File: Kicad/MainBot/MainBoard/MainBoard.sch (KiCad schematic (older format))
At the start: 58 parts, among them J1 Conn_01x02, J10 Conn_01x24, J11 01x24, J12 Conn_01x05, J13 Conn_01x03, J14 Conn_01x03, J15 Conn_01x03, J16 01x04, J17 01x04, J18 01x04, J19 01x04, J20 Conn_01x03, U1 AZ1117-3.3, U2 TCA9548A, U3 Teensy3.6, U4 DRV8825, U5 DRV8825, U6 DRV8825, U7 DRV8825

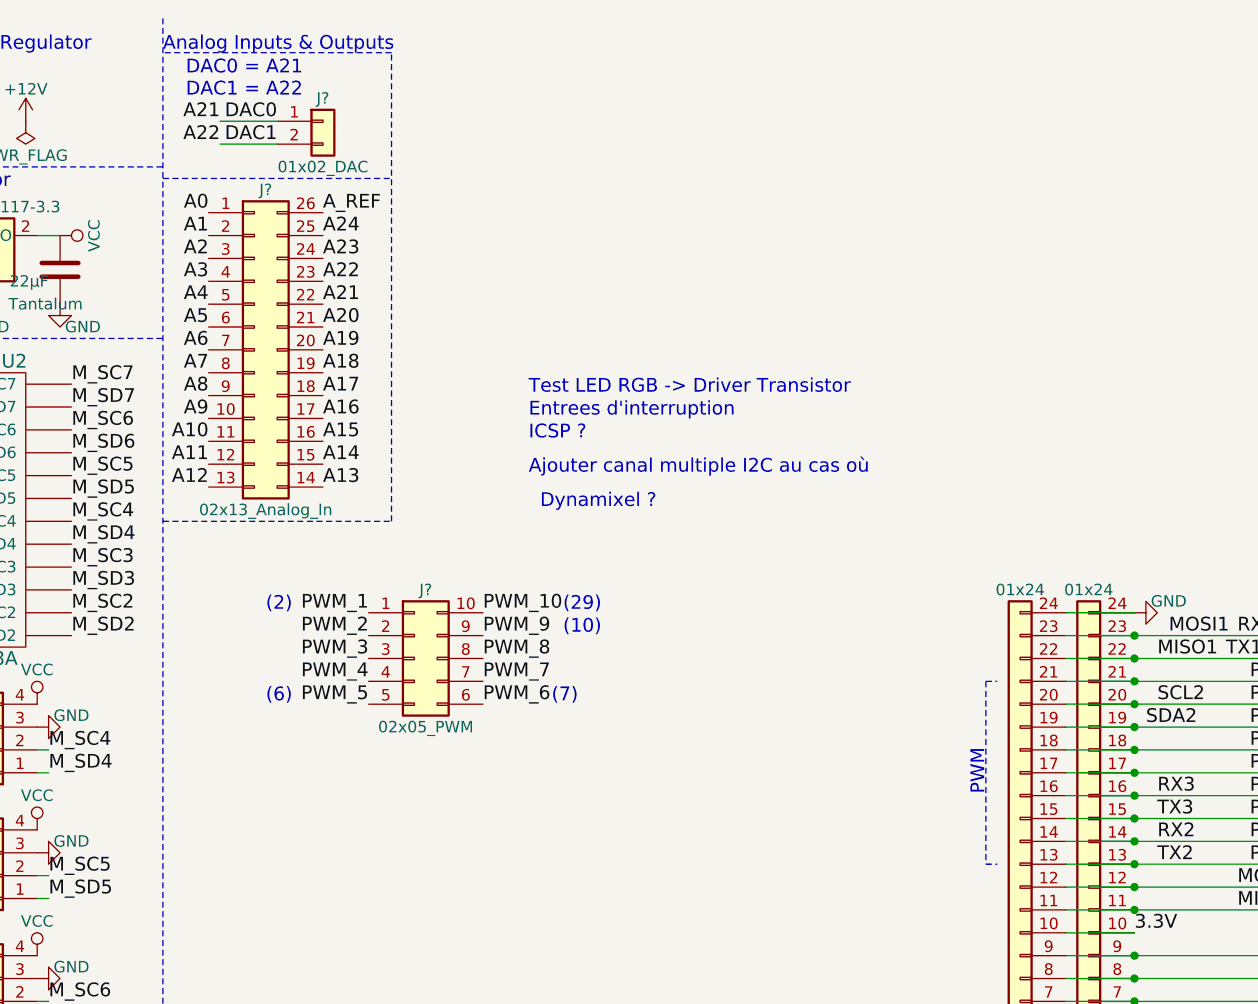
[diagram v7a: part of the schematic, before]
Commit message: Deleted PWM and analog blocks
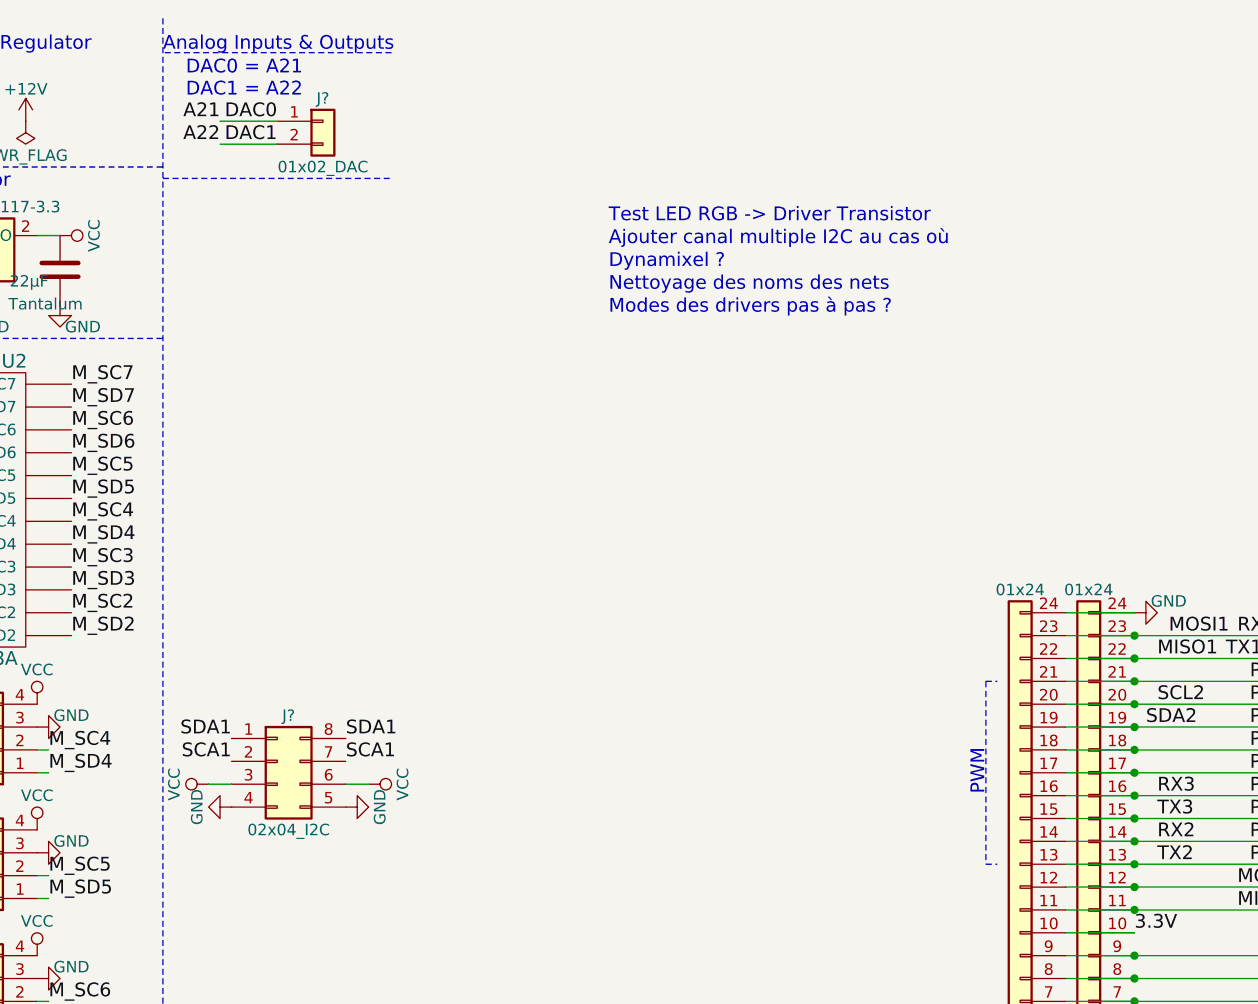
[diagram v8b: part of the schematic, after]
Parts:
- removed J?: 02x13_Analog_In, symbol Conn_02x13_Counter_Clockwise
- removed J?: 02x05_PWM, symbol Conn_02x05_Counter_Clockwise
- added J?: 02x04_I2C, symbol Conn_02x04_Counter_Clockwise
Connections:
- net A19: now also J?.1 (Pin_1), J?.8 (Pin_8)
- net GND: now also J?.4 (Pin_4), J?.5 (Pin_5)
- net VCC: now also J?.3 (Pin_3), J?.6 (Pin_6)
- new net SCA1: J?.2 (Pin_2), J?.7 (Pin_7)
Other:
- note added: "Modes des drivers pas à pas ?\n"
- note added: "Nettoyage des noms des nets\n"
- note removed: "(10)\n"
- note removed: "(2)\n"
- note removed: "(29)\n"
- note removed: "(6)\n"
- note removed: "(7)\n"
- note removed: "Entrees d'interruption\n"
- note removed: "ICSP ?\n"
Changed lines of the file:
@@
 Text Label 850  9400 0    60   ~ 0
 3.3V
-Text Notes 3850 2250 0    60   ~ 0
-Entrees d'interruption\n
-Text Notes 3850 2350 0    60   ~ 0
-ICSP ?\n
-Text Notes 3850 2150 0    60   ~ 0
+Text Notes 4200 1400 0    60   ~ 0
 Test LED RGB -> Driver Transistor\n
 $Comp
@@
 Wire Wire Line
 	9300 6100 9900 6100
-Text Label 2450 1350 2    60   ~ 0
-A0
-Text Label 2450 1450 2    60   ~ 0
-A1
-Text Label 2450 1550 2    60   ~ 0
-A2
-Text Label 2450 1650 2    60   ~ 0
-A3
-Text Label 2450 1750 2    60   ~ 0
-A4
-Text Label 2450 1850 2    60   ~ 0
-A5
-Text Label 2450 1950 2    60   ~ 0
-A6
-Text Label 2450 2050 2    60   ~ 0
-A7
-Text Label 2450 2150 2    60   ~ 0
-A8
-Text Label 2450 2250 2    60   ~ 0
-A9
-Text Label 2450 2350 2    60   ~ 0
-A10
-Text Label 2450 2450 2    60   ~ 0
-A11
-Text Label 2450 2550 2    60   ~ 0
-A12
-Text Label 2950 2550 0    60   ~ 0
-A13
-Text Label 2950 2450 0    60   ~ 0
-A14
-Text Label 2950 2350 0    60   ~ 0
-A15
-Text Label 2950 2250 0    60   ~ 0
-A16
-Text Label 2950 2150 0    60   ~ 0
-A17
-Text Label 2950 2050 0    60   ~ 0
-A18
-Text Label 2950 1950 0    60   ~ 0
-A19
-Text Label 2950 1850 0    60   ~ 0
-A20
-Text Label 2950 1750 0    60   ~ 0
-A21
-Text Label 2950 1650 0    60   ~ 0
-A22
-Text Label 2950 1550 0    60   ~ 0
-A23
-$Comp
-L Conn_02x13_Counter_Clockwise J?
-U 1 1 5C64862D
-P 2650 1950
-F 0 "J?" H 2700 2650 50  0000 C CNN
-F 1 "02x13_Analog_In" H 2700 1250 50  0000 C CNN
-F 2 "" H 2650 1950 50  0001 C CNN
-F 3 "" H 2650 1950 50  0001 C CNN
-	1    2650 1950
-	1    0    0    -1
-$EndComp
-Text Label 2950 1450 0    60   ~ 0
-A24
-Text Label 2950 1350 0    60   ~ 0
-A_REF
 $Comp
 L Conn_01x02 J?
@@
 DAC0 = A21\nDAC1 = A22\n
 Wire Notes Line
-	3250 2700 3250 650
-Wire Notes Line
 	3250 650  2250 650
 Wire Notes Line
@@
 Wire Notes Line
 	5850 4200 5900 4200
-$Comp
-L Conn_02x05_Counter_Clockwise J?
-U 1 1 5C6567B2
-P 3350 3300
-F 0 "J?" H 3400 3600 50  0000 C CNN
-F 1 "02x05_PWM" H 3400 3000 50  0000 C CNN
-F 2 "" H 3350 3300 50  0001 C CNN
-F 3 "" H 3350 3300 50  0001 C CNN
-	1    3350 3300
-	1    0    0    -1
-$EndComp
-Text Label 3150 3100 2    60   ~ 0
-PWM_1
-Text Label 3150 3200 2    60   ~ 0
-PWM_2
-Text Label 3150 3300 2    60   ~ 0
-PWM_3
-Text Label 3150 3400 2    60   ~ 0
-PWM_4
-Text Label 3150 3500 2    60   ~ 0
-PWM_5
-Text Label 3650 3500 0    60   ~ 0
-PWM_6
-Text Label 3650 3400 0    60   ~ 0
-PWM_7
-Text Label 3650 3300 0    60   ~ 0
-PWM_8
-Text Label 3650 3200 0    60   ~ 0
-PWM_9
-Text Label 3650 3100 0    60   ~ 0
-PWM_10
-Wire Notes Line
-	2250 2700 3250 2700
-Text Notes 2700 3100 0    60   ~ 0
-(2)\n
-Text Notes 2700 3500 0    60   ~ 0
-(6)\n
-Text Notes 3950 3500 0    60   ~ 0
-(7)\n
-Text Notes 4000 3100 0    60   ~ 0
-(29)\n
-Text Notes 4000 3200 0    60   ~ 0
-(10)\n
 Wire Notes Line
 	500  6250 1600 6250
@@
 Text Label 950  2800 2    60   ~ 0
 ADDR_2
-Text Notes 3850 2500 0    60   ~ 0
+Text Notes 4200 1500 0    60   ~ 0
 Ajouter canal multiple I2C au cas où\n
-Text Notes 3900 2650 0    60   ~ 0
+Text Notes 4200 1600 0    60   ~ 0
 Dynamixel ?\n
+Text Notes 4200 1700 0    60   ~ 0
+Nettoyage des noms des nets\n
+$Comp
+L Conn_02x04_Counter_Clockwise J?
+U 1 1 5C68FB43
+P 2750 3750
+F 0 "J?" H 2800 3950 50  0000 C CNN
+F 1 "02x04_I2C" H 2800 3450 50  0000 C CNN
+F 2 "" H 2750 3750 50  0001 C CNN
+F 3 "" H 2750 3750 50  0001 C CNN
+	1    2750 3750
+	1    0    0    -1
+$EndComp
+$Comp
+L GND #PWR?
+U 1 1 5C690B58
+P 2550 3950
+F 0 "#PWR?" H 2550 3700 50  0001 C CNN
+F 1 "GND" H 2550 3800 50  0000 C CNN
+F 2 "" H 2550 3950 50  0001 C CNN
+F 3 "" H 2550 3950 50  0001 C CNN
+	1    2550 3950
+	0    1    1    0
+$EndComp
+$Comp
+L GND #PWR?
+U 1 1 5C690D42
+P 3050 3950
+F 0 "#PWR?" H 3050 3700 50  0001 C CNN
+F 1 "GND" H 3050 3800 50  0000 C CNN
+F 2 "" H 3050 3950 50  0001 C CNN
+F 3 "" H 3050 3950 50  0001 C CNN
+	1    3050 3950
+	0    -1   -1   0
+$EndComp
+$Comp
+L VCC #PWR?
+U 1 1 5C690FE2
+P 3150 3850
+F 0 "#PWR?" H 3150 3700 50  0001 C CNN
+F 1 "VCC" H 3150 4000 50  0000 C CNN
+F 2 "" H 3150 3850 50  0001 C CNN
+F 3 "" H 3150 3850 50  0001 C CNN
+	1    3150 3850
+	0    1    1    0
+$EndComp
+$Comp
+L VCC #PWR?
+U 1 1 5C6910A5
+P 2450 3850
+F 0 "#PWR?" H 2450 3700 50  0001 C CNN
+F 1 "VCC" H 2450 4000 50  0000 C CNN
+F 2 "" H 2450 3850 50  0001 C CNN
+F 3 "" H 2450 3850 50  0001 C CNN
+	1    2450 3850
+	0    -1   -1   0
+$EndComp
+Wire Wire Line
+	2450 3850 2550 3850
+Wire Wire Line
+	3050 3850 3150 3850
+Text Label 2550 3650 2    60   ~ 0
+SDA1
+Text Label 3050 3650 0    60   ~ 0
+SDA1
+Text Label 3050 3750 0    60   ~ 0
+SCA1
+Text Label 2550 3750 2    60   ~ 0
+SCA1
+Text Notes 4200 1800 0    60   ~ 0
+Modes des drivers pas à pas ?\n
 $EndSCHEMATC
